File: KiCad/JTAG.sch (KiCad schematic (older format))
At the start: 2 parts, among them CON1 AVR-JTAG-10, J19 CONN_ARM_JTAG_SWD_20

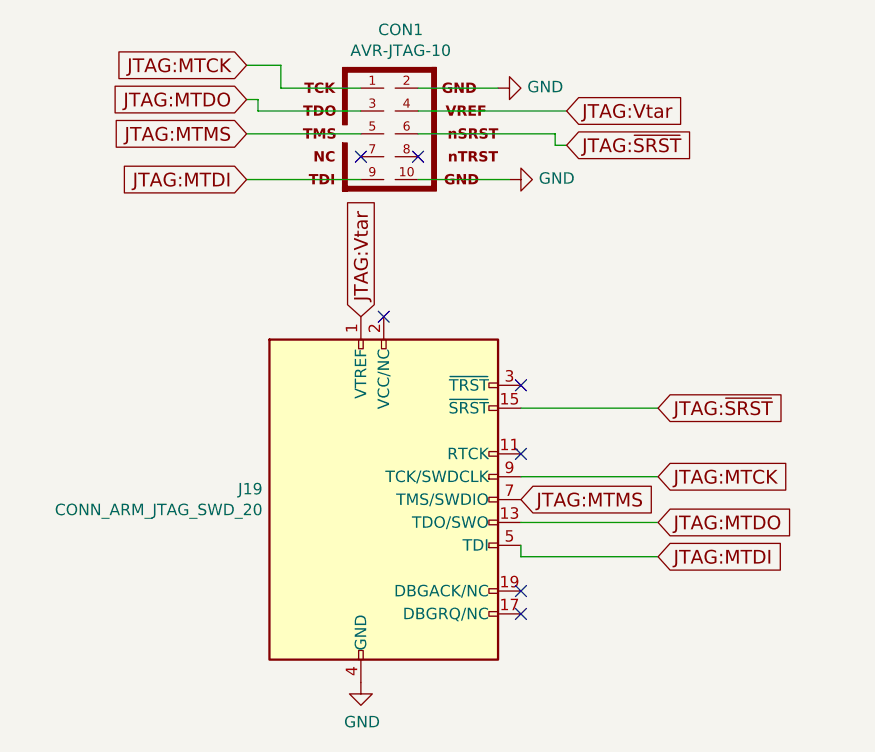
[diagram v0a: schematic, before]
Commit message: Use I2C for I/O
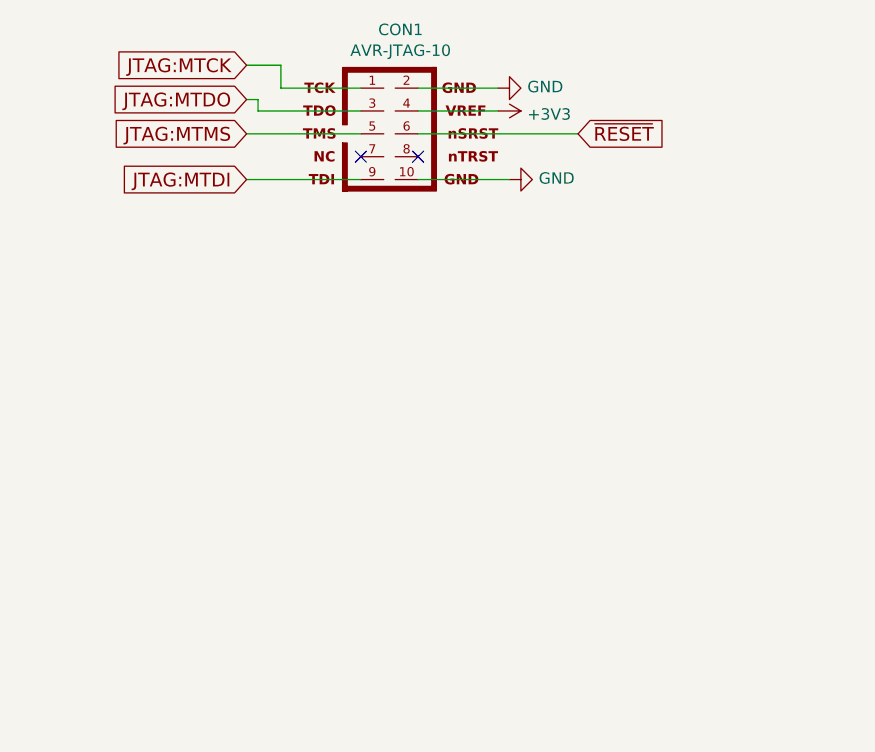
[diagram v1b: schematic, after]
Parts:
- removed J19: CONN_ARM_JTAG_SWD_20, Connectors:IDC_Header_Straight_20pins, symbol CONN_ARM_JTAG_SWD_20
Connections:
- net JTAG:Vtar renamed +3V3
- net JTAG:~SRST renamed ~RESET
- no-connect marks 7 -> 2
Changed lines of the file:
@@
 LIBS:ESD_Protection
 LIBS:SRR1260-330M
+LIBS:ADS1115IDGST
 LIBS:HAP-IO-Card-cache
 EELAYER 26 0
@@
 Text GLabel 3600 2900 0    60   Input ~ 0
 JTAG:MTMS
-Text GLabel 5000 2800 2    60   Input ~ 0
-JTAG:Vtar
-Text GLabel 5000 2950 2    60   Input ~ 0
-JTAG:~SRST
+Text GLabel 5050 2900 2    60   Input ~ 0
+~RESET
 $Comp
 L AVR-JTAG-10 CON1
@@
 $EndComp
 $Comp
-L GND #PWR042
+L GND #PWR081
 U 1 1 591CB17E
 P 4750 3100
-F 0 "#PWR042" H 4750 2850 50  0001 C CNN
+F 0 "#PWR081" H 4750 2850 50  0001 C CNN
 F 1 "GND" V 4755 2972 50  0000 R CNN
 F 2 "" H 4750 3100 50  0001 C CNN
@@
 $EndComp
 NoConn ~ 4100 3000
-$Comp
-L CONN_ARM_JTAG_SWD_20 J19
-U 1 1 591CB43D
-P 4200 4500
-F 0 "J19" H 3670 4546 50  0000 R CNN
-F 1 "CONN_ARM_JTAG_SWD_20" H 3670 4455 50  0000 R CNN
-F 2 "Connectors:IDC_Header_Straight_20pins" H 4650 3450 50  0001 L TNN
-F 3 "" V 3850 3250 50  0001 C CNN
-	1    4200 4500
-	1    0    0    -1
-$EndComp
 Wire Wire Line
-	4350 2900 4950 2900
+	4350 2900 5050 2900
 Wire Wire Line
 	3750 2700 4100 2700
@@
 	3650 2800 4100 2800
 Wire Wire Line
-	5000 2800 4350 2800
-Wire Wire Line
-	4950 2900 4950 2950
-Wire Wire Line
-	4950 2950 5000 2950
+	4700 2800 4350 2800
 Wire Wire Line
 	3750 2700 3750 2600
@@
 Wire Wire Line
 	3650 2750 3600 2750
-Text GLabel 5400 4750 2    60   Input ~ 0
-JTAG:MTDI
-Text GLabel 5400 4600 2    60   Input ~ 0
-JTAG:MTDO
-Text GLabel 5400 4400 2    60   Input ~ 0
-JTAG:MTCK
-Text GLabel 4800 4500 2    60   Input ~ 0
-JTAG:MTMS
-Text GLabel 5400 4100 2    60   Input ~ 0
-JTAG:~SRST
-Text GLabel 4100 3700 1    60   Input ~ 0
-JTAG:Vtar
-Wire Wire Line
-	5400 4600 4800 4600
-Wire Wire Line
-	5400 4100 4800 4100
-Wire Wire Line
-	5400 4400 4800 4400
-Wire Wire Line
-	5400 4750 4800 4750
-Wire Wire Line
-	4800 4750 4800 4700
-$Comp
-L GND #PWR043
-U 1 1 591CB909
-P 4100 5300
-F 0 "#PWR043" H 4100 5050 50  0001 C CNN
-F 1 "GND" H 4105 5127 50  0000 C CNN
-F 2 "" H 4100 5300 50  0001 C CNN
-F 3 "" H 4100 5300 50  0001 C CNN
-	1    4100 5300
-	1    0    0    -1
-$EndComp
-NoConn ~ 4800 4900
-NoConn ~ 4800 5000
-NoConn ~ 4800 4300
 Wire Wire Line
 	3650 2800 3650 2750
-NoConn ~ 4800 4000
 NoConn ~ 4350 3000
 $Comp
-L GND #PWR044
+L GND #PWR082
 U 1 1 591D5632
 P 4700 2700
-F 0 "#PWR044" H 4700 2450 50  0001 C CNN
+F 0 "#PWR082" H 4700 2450 50  0001 C CNN
 F 1 "GND" V 4705 2572 50  0000 R CNN
 F 2 "" H 4700 2700 50  0001 C CNN
@@
 	0    -1   -1   0
 $EndComp
-NoConn ~ 4200 3700
+$Comp
+L +3V3 #PWR083
+U 1 1 592C5156
+P 4700 2800
+F 0 "#PWR083" H 4700 2650 50  0001 C CNN
+F 1 "+3V3" V 4715 2928 50  0000 L CNN
+F 2 "" H 4700 2800 50  0001 C CNN
+F 3 "" H 4700 2800 50  0001 C CNN
+	1    4700 2800
+	0    1    1    0
+$EndComp
 $EndSCHEMATC
